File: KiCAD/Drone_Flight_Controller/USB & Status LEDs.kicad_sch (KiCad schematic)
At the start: 25 parts, among them P1 USB_C_Plug_USB2.0, Q11 BC546, Q13 BC546, Q14 BC546, Q16 BC546, Q18 BC546, Q21 BC546, Q22 BC546, U5 MCP2200-I-SO, Y2 CSTNE12M0GH5L000R0

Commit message: Fix Label Error
Fix Label Error
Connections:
- net +3V3 renamed +3.0V
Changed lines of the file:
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@@
 			)
 		)
-		(property "Value" "+3V3"
+		(property "Value" "+3.0V"
 			(at 133.35 38.1 0)
 			(effects

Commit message: Reanotate
Reanotate
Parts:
- renumbered D4 to D701, D5 to D702, D7 to D703, D8 to D704, D9 to D705, D2 to D706, D3 to D707, P1 to P701, Q11 to Q701, Q13 to Q702, Q14 to Q703, Q16 to Q704, Q18 to Q705, Q21 to Q706, Q22 to Q707, R20 to R701, R28 to R702, R29 to R703, R30 to R704, R31 to R705, R32 to R706, R33 to R707, R34 to R708, U5 to U701, Y2 to Y701

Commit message: Reannotate
Reannotate
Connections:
- net +3.0V renamed +3.3V
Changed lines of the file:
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@@
 		(dnp no)
 		(fields_autoplaced yes)
-		(property "Reference" "#PWR0701"
+		(property "Reference" "#PWR0706"
 			(at 76.2 95.25 0)
 			(effects
@@
 			(project "Drone_Flight_Controller"
 				(path "/05daaa24-e506-4b9a-9564-8bf799413ca8/8421779c-d2a0-463b-acfb-bef6fd845f5d"
-					(reference "#PWR0701")
+					(reference "#PWR0706")
 					(unit 1)
 				)
@@
 		(on_board yes)
 		(dnp no)
-		(property "Reference" "#PWR0706"
+		(property "Reference" "#PWR0703"
 			(at 198.12 52.07 0)
 			(effects
@@
 			(project "Drone_Flight_Controller"
 				(path "/05daaa24-e506-4b9a-9564-8bf799413ca8/8421779c-d2a0-463b-acfb-bef6fd845f5d"
-					(reference "#PWR0706")
+					(reference "#PWR0703")
 					(unit 1)
 				)
@@
 		(dnp no)
 		(fields_autoplaced yes)
-		(property "Reference" "#PWR0703"
+		(property "Reference" "#PWR0701"
 			(at 93.98 46.99 0)
 			(effects
@@
 			(project "Drone_Flight_Controller"
 				(path "/05daaa24-e506-4b9a-9564-8bf799413ca8/8421779c-d2a0-463b-acfb-bef6fd845f5d"
-					(reference "#PWR0703")
+					(reference "#PWR0701")
 					(unit 1)
 				)
@@
 		(dnp no)
 		(fields_autoplaced yes)
-		(property "Reference" "#PWR0704"
+		(property "Reference" "#PWR0708"
 			(at 130.81 105.41 0)
 			(effects
@@
 			(project "Drone_Flight_Controller"
 				(path "/05daaa24-e506-4b9a-9564-8bf799413ca8/8421779c-d2a0-463b-acfb-bef6fd845f5d"
-					(reference "#PWR0704")
+					(reference "#PWR0708")
 					(unit 1)
 				)
@@
 		(on_board yes)
 		(dnp no)
-		(property "Reference" "#PWR0708"
+		(property "Reference" "#PWR0704"
 			(at 218.44 52.07 0)
 			(effects
@@
 			(project ""
 				(path "/05daaa24-e506-4b9a-9564-8bf799413ca8/8421779c-d2a0-463b-acfb-bef6fd845f5d"
-					(reference "#PWR0708")
+					(reference "#PWR0704")
 					(unit 1)
 				)
@@
 		(dnp no)
 		(fields_autoplaced yes)
-		(property "Reference" "#PWR0707"
+		(property "Reference" "#PWR0709"
 			(at 198.12 163.83 0)
 			(effects
@@
 			(project "Drone_Flight_Controller"
 				(path "/05daaa24-e506-4b9a-9564-8bf799413ca8/8421779c-d2a0-463b-acfb-bef6fd845f5d"
-					(reference "#PWR0707")
+					(reference "#PWR0709")
 					(unit 1)
 				)
@@
 		(dnp no)
 		(fields_autoplaced yes)
-		(property "Reference" "#PWR0709"
+		(property "Reference" "#PWR0710"
 			(at 218.44 153.67 0)
 			(effects
@@
 			(project "Drone_Flight_Controller"
 				(path "/05daaa24-e506-4b9a-9564-8bf799413ca8/8421779c-d2a0-463b-acfb-bef6fd845f5d"
-					(reference "#PWR0709")
+					(reference "#PWR0710")
 					(unit 1)
 				)
@@
 		(dnp no)
 		(fields_autoplaced yes)
-		(property "Reference" "#PWR0702"
+		(property "Reference" "#PWR0707"
 			(at 90.17 95.25 0)
 			(effects
@@
 			(project "Drone_Flight_Controller"
 				(path "/05daaa24-e506-4b9a-9564-8bf799413ca8/8421779c-d2a0-463b-acfb-bef6fd845f5d"
-					(reference "#PWR0702")
+					(reference "#PWR0707")
 					(unit 1)
 				)
@@
 		(on_board yes)
 		(dnp no)
-		(property "Reference" "#PWR0710"
+		(property "Reference" "#PWR0705"
 			(at 248.92 52.07 0)
 			(effects
@@
 			(project "Drone_Flight_Controller"
 				(path "/05daaa24-e506-4b9a-9564-8bf799413ca8/8421779c-d2a0-463b-acfb-bef6fd845f5d"
-					(reference "#PWR0710")
+					(reference "#PWR0705")
 					(unit 1)
 				)
@@
 		(dnp no)
 		(fields_autoplaced yes)
-		(property "Reference" "#PWR0705"
+		(property "Reference" "#PWR0702"
 			(at 133.35 46.99 0)
 			(effects
@@
 			)
 		)
-		(property "Value" "+3.0V"
+		(property "Value" "+3.3V"
 			(at 133.35 38.1 0)
 			(effects
@@
 			(project ""
 				(path "/05daaa24-e506-4b9a-9564-8bf799413ca8/8421779c-d2a0-463b-acfb-bef6fd845f5d"
-					(reference "#PWR0705")
-					(unit 1)
-				)
+					(reference "#PWR0702")
+					(unit 1)
+				)

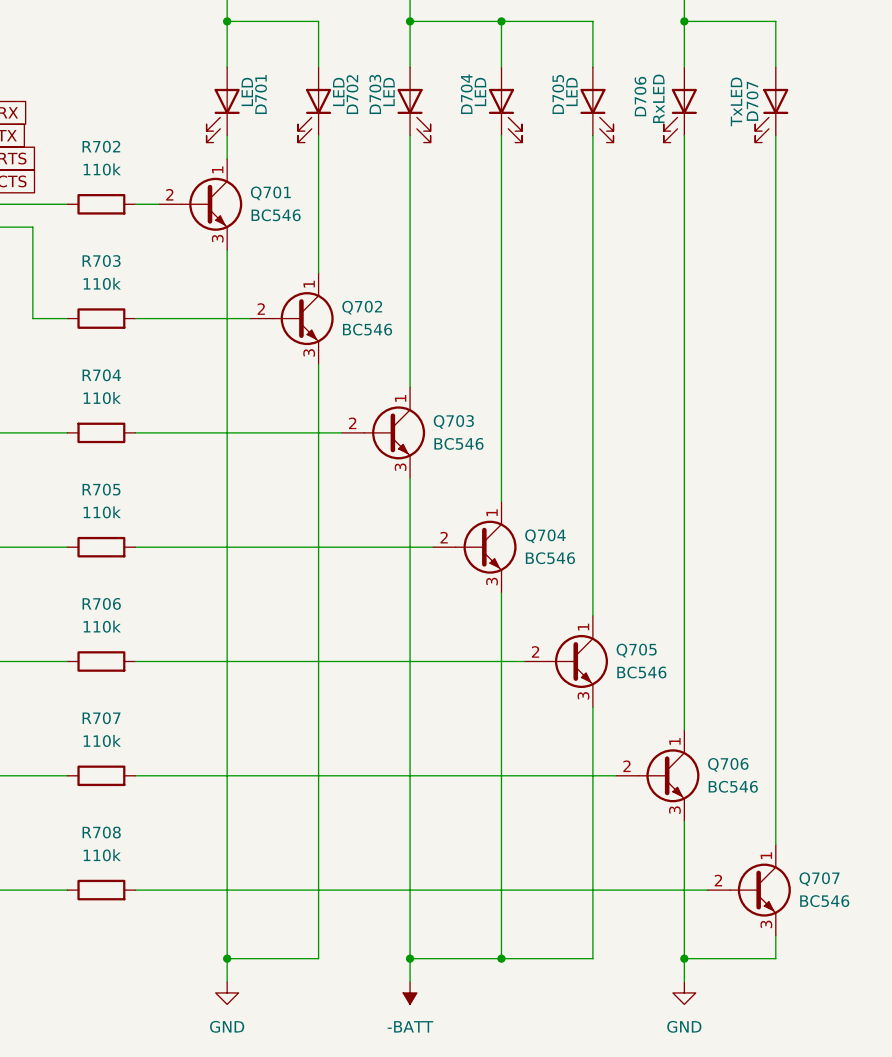
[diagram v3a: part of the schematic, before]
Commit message: Change Transistors to SMD Variants
Change Transistors to SMD Variants
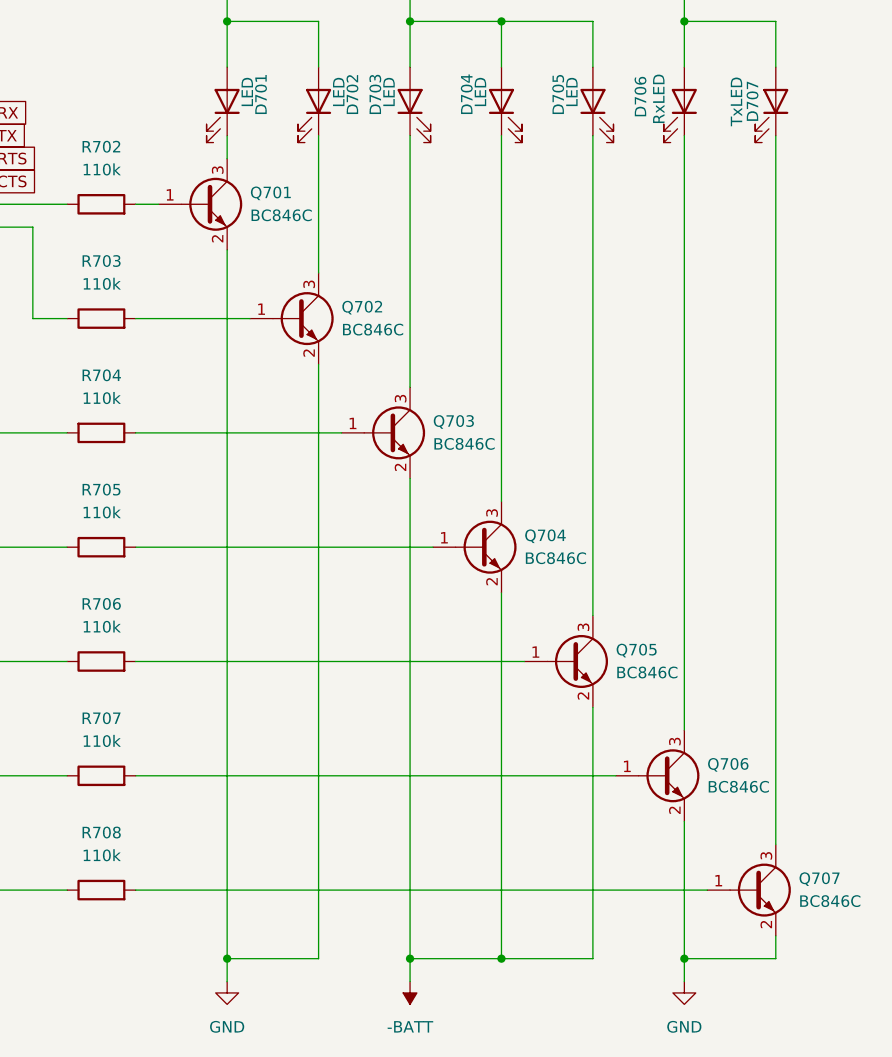
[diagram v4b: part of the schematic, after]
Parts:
- removed Q701, Q702, Q703, Q704, Q705, Q706, Q707: BC546, Package_TO_SOT_THT:TO-92_Inline, symbol Transistor_BJT:BC546
- added Q701, Q702, Q703, Q704, Q705, Q706, Q707: BC846C, Package_TO_SOT_SMD:SOT-23, symbol Transistor_BJT:BC846
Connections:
- net -BATT: now also Q703.2 (E), Q704.2 (E), Q705.2 (E)
- net GND: now also Q701.2 (E), Q702.2 (E), Q706.2 (E), Q707.2 (E)
- net at D702.1 (K): now also Q702.3 (C)
- net at D701.1 (K): now also Q701.3 (C)
- net at R706.2: now also Q705.1 (B)
- net at D704.1 (K): now also Q704.3 (C)
- net at D706.1 (K): now also Q706.3 (C)
- net at R707.2: now also Q706.1 (B)
- net at D707.1 (K): now also Q707.3 (C)
- net at R702.2: now also Q701.1 (B)
- net at D703.1 (K): now also Q703.3 (C)
- net at R704.1: now also Q703.1 (B)
- net at R708.2: now also Q707.1 (B)
- net at R703.2: now also Q702.1 (B)
- net at R705.2: now also Q704.1 (B)
- net at D705.1 (K): now also Q705.3 (C)
